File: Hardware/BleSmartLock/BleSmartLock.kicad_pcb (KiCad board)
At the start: 2 copper layers, 119 parts, among them J1 Conn_01x02, J10 Conn_01x04, J11 Conn_01x04, J12 Conn_01x02, J2 Conn_01x01, J3 Conn_01x01, J4 Conn_01x01, J5 Conn_01x01, J6 Conn_ST_STDC14, J7 Conn_01x06, J8 Conn_01x03, J9 Conn_01x04, Q1 PMV50UPE, Q10 NX7002AKA, Q11 PMV50UPE, Q12 NX7002AKA, Q13 NX7002AKA, Q14 NX7002AKA, Q2 PMV50UPE, Q3 NX7002AKA, Q4 PMV50UPE, Q5 NX7002AKA, Q6 NX7002AKA, Q7 PMV50UPE, Q8 NX7002AKA, Q9 PMV50UPE, SW1 SW_Push, U1 RT9086, U2 XC9264b755, U3 BLUENRG-M2SA, U4 LMV611

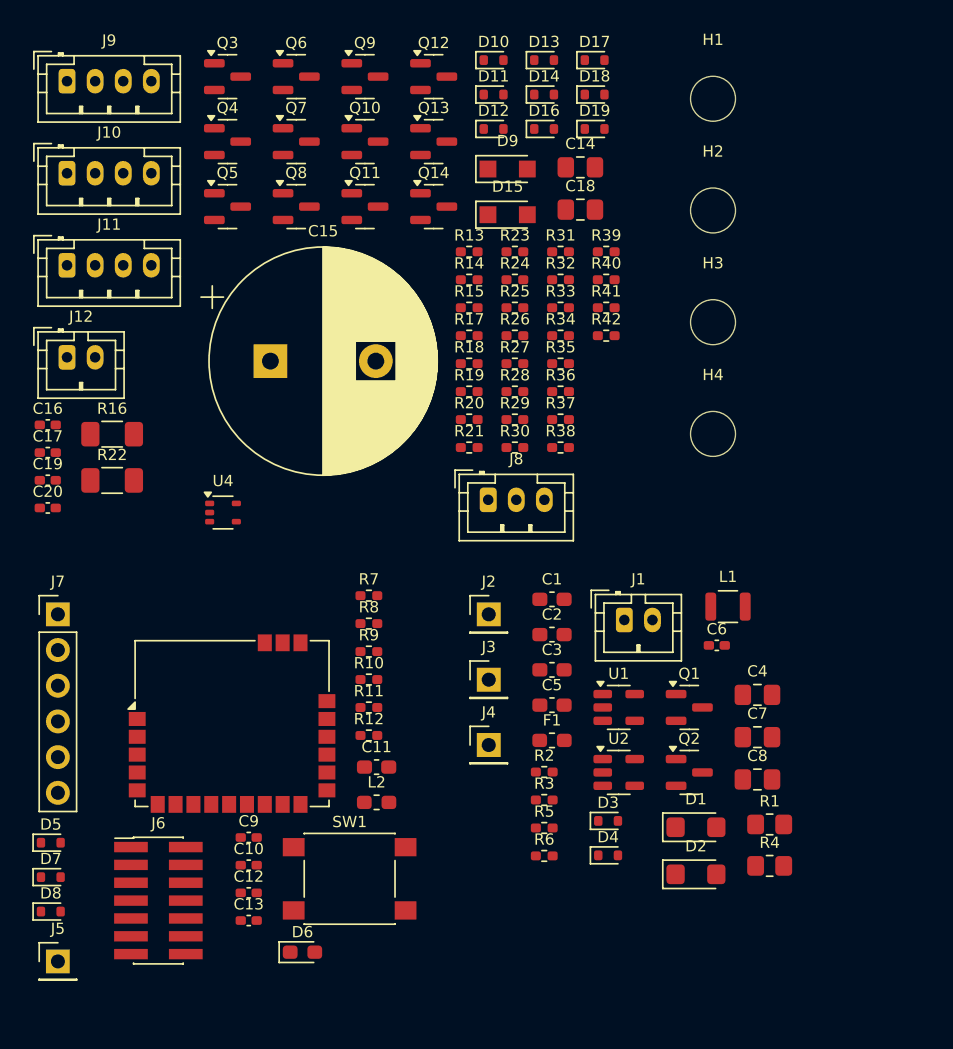
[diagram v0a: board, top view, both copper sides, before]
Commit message: Ajout carte BleSmartLock
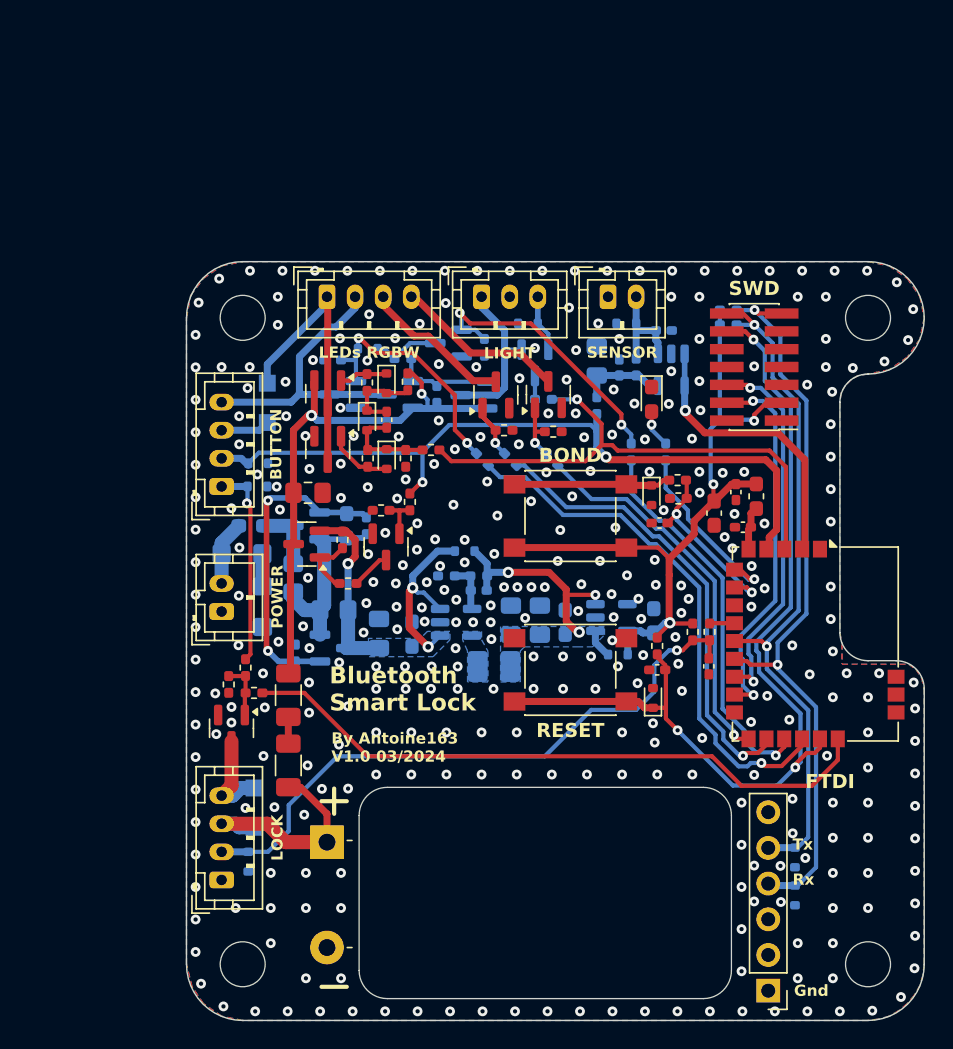
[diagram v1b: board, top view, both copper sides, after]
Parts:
- removed J2, J3, J4, J5: Conn_01x01, Connector_PinHeader_2.54mm:PinHeader_1x01_P2.54mm_Vertical
- removed R42: 160K, Resistor_SMD:R_0402_1005Metric_Pad0.72x0.64mm_HandSolder
- added D20: ESD5Z3.3T1G, Diode_SMD:D_SOD-523, B.Cu at (167.8, 80.9)
- added SW2: SW_Push, Button_Switch_SMD:SW_SPST_PTS645, F.Cu at (163.8, 94.6)
- C1, C18, C19, C2, C20, C3, C4, C5, C6, C7, C8, D1, D2, D3, D4, D8, F1, Q1, Q10, Q11, Q12, Q2, Q5, Q9, R1, R10, R11, R12, R17, R2, R3, R30, R31, R32, R33, R4, R5, R6, U1, U2: moved to B.Cu
- C15: footprint Capacitor_THT:CP_Radial_D16.0mm_P7.50mm -> AM163:CP_Radial_L25.0mm_D16.0mm_P7.50mm_Horizontal_EdgeCuts
- D10, D16: value ESD5Z3.3T1G -> PMEG40T10ER; footprint Diode_SMD:D_SOD-523 -> Diode_SMD:Nexperia_CFP3_SOD-123W; moved to B.Cu
- D11: value EDZVT2R9.1B -> ESD5Z3.3T1G; moved to B.Cu
- D12: value RB501SM-30FH -> EDZVT2R9.1B
- D14: value ESD5Z3.3T1G -> RB501SM-30FH
- D15, D9: value PMEG40T10ER -> ESD5Z3.3T1G; footprint Diode_SMD:Nexperia_CFP3_SOD-123W -> Diode_SMD:D_SOD-523; moved to B.Cu
- D17: value ESD5Z3.3T1G -> ESD5Z3.3T1G; moved to B.Cu
- D18: value RB501SM-30FH -> ESD5Z3.3T1G; moved to B.Cu
- D19: value ESD5Z3.3T1G -> RB501SM-30FH; moved to B.Cu
- D6: value LED -> ESD5Z3.3T1G; footprint LED_SMD:LED_0603_1608Metric_Pad1.05x0.95mm_HandSolder -> Diode_SMD:D_SOD-523
- D7: value ESD5Z3.3T1G -> LED; footprint Diode_SMD:D_SOD-523 -> LED_SMD:LED_0603_1608Metric_Pad1.05x0.95mm_HandSolder
- L1: footprint AM163:L_TDK_VLS252012HBX_Handsoldering -> Inductor_SMD:L_1008_2520Metric_Pad1.43x2.20mm_HandSolder; moved to B.Cu
- Q6: value NX7002AKA -> PMV52ENEA
- R34: value R -> 1K; moved to B.Cu
- R35: value 1K -> 100K; moved to B.Cu
- R36, R38, R40: value 100K -> 1K; moved to B.Cu
- R37, R39: value 1K -> 100K
- R41: value 1K -> 160K; moved to B.Cu
- U4: footprint Package_TO_SOT_SMD:SOT-353_SC-70-5 -> Package_TO_SOT_SMD:SOT-23-5; moved to B.Cu
- moved D17 62.1 mm to (140.9, 119.2), turned to -90 degrees
- moved J7 57.2 mm to (177.9, 128.4), turned to 180 degrees
- moved J6 56.9 mm to (176.9, 84.0), turned to 180 degrees
- moved D10 55.9 mm to (141.3, 115.4), turned to 90 degrees
- moved D9 55.6 mm to (179.8, 121.6), turned to -90 degrees
- moved D7 54.6 mm to (169.6, 86.3), turned to -90 degrees
- moved D8 53.1 mm to (179.8, 118.9), turned to -90 degrees
- moved J10 51.5 mm to (139.0, 120.5), turned to 90 degrees
- moved H4 50.4 mm to (140.5, 126.5)
- moved C17 49.4 mm to (173.7, 105.3), turned to -90 degrees
- moved H3 47.0 mm to (185.0, 126.5)
- moved Q6 46.6 mm to (139.7, 109.7), turned to -90 degrees
- moved C20 45.6 mm to (170.5, 81.4)
- moved C13 44.9 mm to (176.1, 95.4), turned to 180 degrees
- moved C12 44.9 mm to (175.6, 92.9), turned to -90 degrees
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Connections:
- C16 pad 1: Net-(D11-K) -> Net-(D12-K)
- C16 pad 2: Net-(D11-A) -> Net-(D12-A)
- C17 pad 1: Net-(D16-K) -> Net-(D17-K)
- C20 pad 1: Net-(D19-K) -> Net-(D20-K)
- D10 pad 1: /InOut/EX_LIGHT_CMD -> /InOut/COIL_P
- D10 pad 2: GND -> /InOut/COIL_N
- D11 pad 1: Net-(D11-K) -> /InOut/EX_LIGHT_CMD
- D11 pad 2: Net-(D11-A) -> GND
- D12 pad 2: Net-(D11-K) -> Net-(D12-A)
- D13 pad 1: Net-(D11-A) -> Net-(D13-K)
- D13 pad 2: Net-(D13-A) -> Net-(D12-K)
- D14 pad 1: /Bluenrg/EN_IO -> Net-(D12-A)
- D14 pad 2: GND -> Net-(D14-A)
- D15 pad 1: /InOut/BP_LED_P -> /Bluenrg/EN_IO
- D15 pad 2: /InOut/AM_LIGHT_12V_W- -> GND
- D16 pad 1: Net-(D16-K) -> /InOut/BP_LED_P
- D16 pad 2: GND -> /InOut/AM_LIGHT_12V_W-
- D17 pad 1: /InOut/BP_NO -> Net-(D17-K)
- D18 pad 1: Net-(D18-K) -> /InOut/BP_NO
- D18 pad 2: Net-(D18-A) -> GND
- D19 pad 2: GND -> Net-(D19-A)
- D5 pad 1: Net-(D5-K) -> /Bluenrg/M2_~{RESET}
- D6 pad 1: GND -> Net-(D6-K)
- D6 pad 2: Net-(D6-A) -> GND
- D7 pad 1: /Bluenrg/UART_TX -> GND
- D7 pad 2: GND -> Net-(D7-A)
- D8 pad 1: /Bluenrg/UART_RX -> /Bluenrg/UART_TX
- D9 pad 1: /InOut/COIL_P -> /Bluenrg/UART_RX
- D9 pad 2: /InOut/COIL_N -> GND
- J1 pad 1: Net-(D1-A2) -> GND
- J1 pad 2: GND -> Net-(D1-A2)
- J10 pad 2: Net-(D16-K) -> Net-(D17-K)
- J10 pad 3: /InOut/COIL_N -> /InOut/COIL_P
- J10 pad 4: /InOut/COIL_P -> /InOut/COIL_N
- J11 pad 1: /InOut/AM_LIGHT_G -> /InOut/AM_LIGHT_12V_W-
- J11 pad 2: /InOut/AM_LIGHT_R -> /InOut/AM_LIGHT_B_W+
- J11 pad 3: /InOut/AM_LIGHT_B_W+ -> /InOut/AM_LIGHT_G
- J11 pad 4: /InOut/AM_LIGHT_12V_W- -> /InOut/AM_LIGHT_R
- J12 pad 2: Net-(D19-K) -> Net-(D20-K)
- J9 pad 3: /InOut/AM_LIGHT_B_W+ -> /InOut/BP_LED_P
- J9 pad 4: /InOut/BP_LED_P -> /InOut/AM_LIGHT_B_W+
- Q10 pad 1: Net-(D18-A) -> Net-(D19-A)
- Q12 pad 3: Net-(D18-K) -> Net-(D19-K)
- Q7 pad 1: Net-(D12-K) -> Net-(D13-K)
- Q8 pad 1: Net-(D13-A) -> Net-(D14-A)
- R10 pad 2: Net-(D6-A) -> Net-(D7-A)
- R23 pad 2: Net-(D11-A) -> Net-(D12-A)
- R24 pad 2: Net-(D11-K) -> Net-(D12-K)
- R25 pad 1: Net-(D11-A) -> Net-(D12-A)
- R26 pad 1: Net-(D11-K) -> Net-(D12-K)
- R26 pad 2: Net-(D12-K) -> Net-(D13-K)
- R27 pad 1: Net-(D11-A) -> Net-(D12-A)
- R27 pad 2: Net-(D13-A) -> Net-(D14-A)
- R28 pad 2: Net-(D16-K) -> Net-(D17-K)
- R29 pad 1: Net-(D16-K) -> Net-(D17-K)
- R31 pad 2: Net-(D18-K) -> Net-(D19-K)
- R32 pad 1: Net-(D18-A) -> Net-(D19-A)
- R33 pad 2: Net-(D18-A) -> Net-(D19-A)
- R34 pad 1: +3V3 -> /Bluenrg/EN_IO
- R35 pad 1: /Bluenrg/EN_IO -> Net-(Q12-G)
- R35 pad 2: Net-(U4-V+) -> GND
- R36 pad 1: Net-(Q12-G) -> /Bluenrg/LIGHT_WHITE
- R36 pad 2: GND -> Net-(Q12-G)
- R37 pad 1: /Bluenrg/LIGHT_WHITE -> Net-(Q13-G)
- R37 pad 2: Net-(Q12-G) -> GND
- R38 pad 1: Net-(Q13-G) -> /Bluenrg/LIGHT_RED
- R38 pad 2: GND -> Net-(Q13-G)
- R39 pad 1: /Bluenrg/LIGHT_RED -> Net-(Q14-G)
- R39 pad 2: Net-(Q13-G) -> GND
- R40 pad 2: GND -> /Bluenrg/LIGHT_GREEN
- R41 pad 1: Net-(Q14-G) -> Net-(U4-V+)
- R41 pad 2: /Bluenrg/LIGHT_GREEN -> Net-(D20-K)
- R8 pad 1: Net-(D5-K) -> Net-(D6-K)
- SW1 pad 1: +3V3 -> /Bluenrg/M2_~{RESET}
- SW1 pad 2: Net-(D5-K) -> GND
- U3 pad 1: /Bluenrg/ADC2 -> unconnected-(U3-ADC2-Pad1)
- U3 pad 16: /Bluenrg/LIGHT_BLUE -> /Bluenrg/LIGHT_GREEN
- U3 pad 17: /Bluenrg/LIGHT_PWM -> /Bluenrg/LIGHT_WHITE
- U3 pad 18: /Bluenrg/LIGHT_GREEN -> /Bluenrg/LIGHT_BLUE
- U3 pad 20: /Bluenrg/OPENED -> /Bluenrg/~{LOCK}
- U3 pad 3: /Bluenrg/LIGHT_WHITE -> /Bluenrg/LIGHT_PWM
- U3 pad 9: /Bluenrg/~{LOCK} -> /Bluenrg/OPENED
- U4 pad 1: Net-(D19-K) -> Net-(D20-K)
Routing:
- net /Bluenrg/M2_~{RESET}: track 0.00 -> 66.8 mm, vias 0 -> 3
- net /Bluenrg/EN_IO: track 0.00 -> 53.6 mm, vias 0 -> 2
- net /Bluenrg/UART_RX: track 0.00 -> 53.1 mm, vias 0 -> 2
- net +3V3: track 0.00 -> 52.3 mm, vias 0 -> 3
- net /Bluenrg/UART_TX: track 0.00 -> 48.9 mm, vias 0 -> 2
- net /Bluenrg/~{LOCK}: track 0.00 -> 46.0 mm
- net Net-(D17-K): track 0.00 -> 44.4 mm, vias 0 -> 1
- net /InOut/POWER_IO_12V: track 0.00 -> 38.3 mm, vias 0 -> 2
- net /Bluenrg/LIGHT_BLUE: track 0.00 -> 38.3 mm, vias 0 -> 1
- net /Bluenrg/LIGHT_PWM: track 0.00 -> 37.4 mm, vias 0 -> 1
- net /Bluenrg/LIGHT_GREEN: track 0.00 -> 32.5 mm, vias 0 -> 1
- net /Bluenrg/LIGHT_WHITE: track 0.00 -> 27.6 mm, vias 0 -> 1
- net /Bluenrg/LIGHT_RED: track 0.00 -> 27.3 mm, vias 0 -> 1
- net /Bluenrg/M2_SWDIO: track 0.00 -> 26.7 mm, vias 0 -> 2
- net /Bluenrg/M2_SWDCLK: track 0.00 -> 26.7 mm, vias 0 -> 2
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- added copper zone on B.Cu, net +12V
- added copper zone on B.Cu, net /Power/3V6
- added copper zone on B.Cu, net GND
- added copper zone on F.Cu, net GND
- added copper zone on B.Cu, net Net-(U2-Lx)
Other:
- board outline added: 52.5 x 54 mm
- board text added: "BOND"
- board text added: "BUTTON"
- board text added: "Bluetooth Smart Lock"
- board text added: "By Antoine163 V1.0 03/2024"
- board text added: "FTDI"
- board text added: "Gnd"
- board text added: "LEDs RGBW"
- board text added: "LIGHT"
- board text added: "LOCK"
- board text added: "POWER"
- board text added: "RESET"
- board text added: "Rx"
- board text added: "SENSOR"
- board text added: "SWD"
- board text added: "Tx"

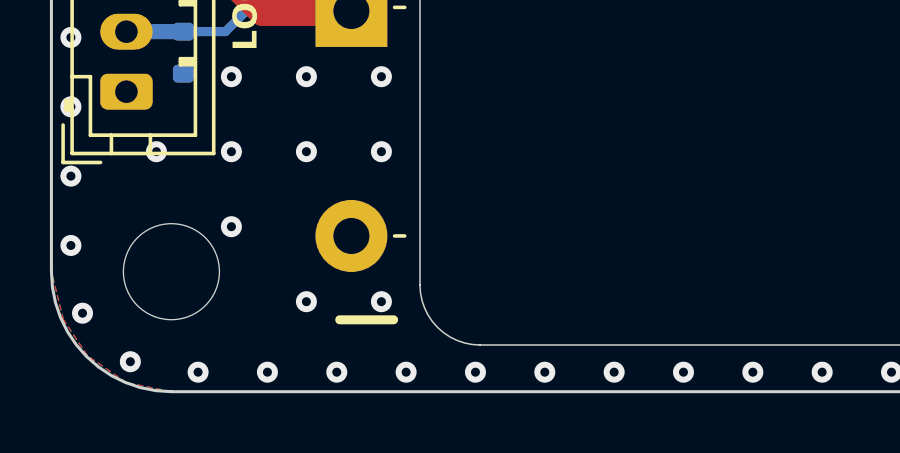
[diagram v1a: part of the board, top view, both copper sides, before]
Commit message: Ajout fichier de production et bom interactive
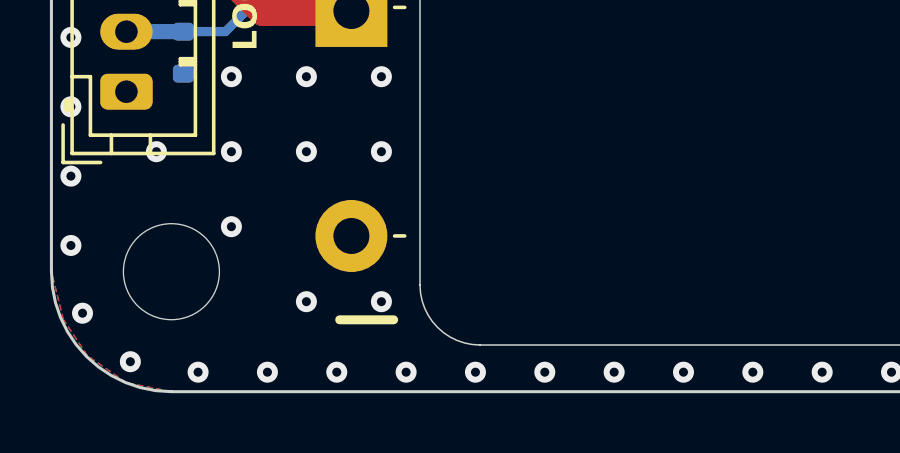
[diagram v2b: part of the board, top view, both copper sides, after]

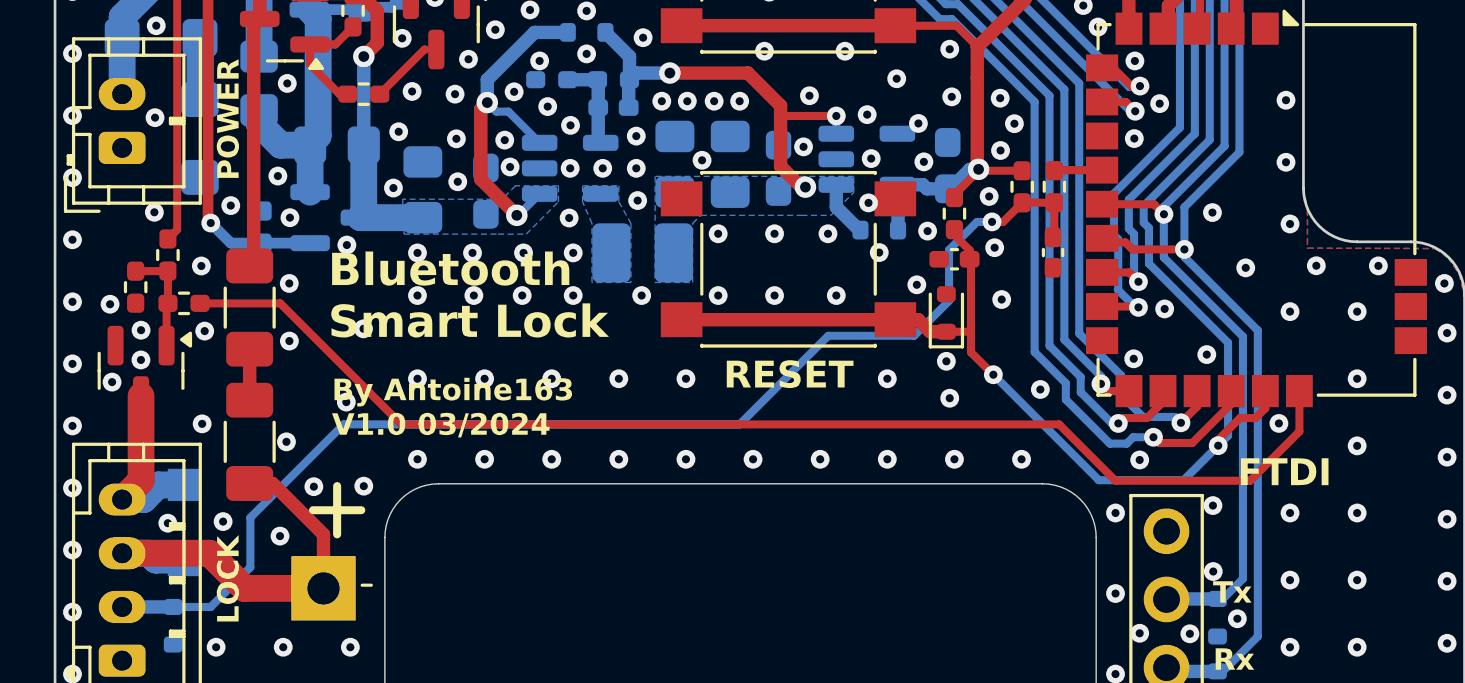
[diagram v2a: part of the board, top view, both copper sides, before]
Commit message: Mise a jour pcb en v1.1 et readme
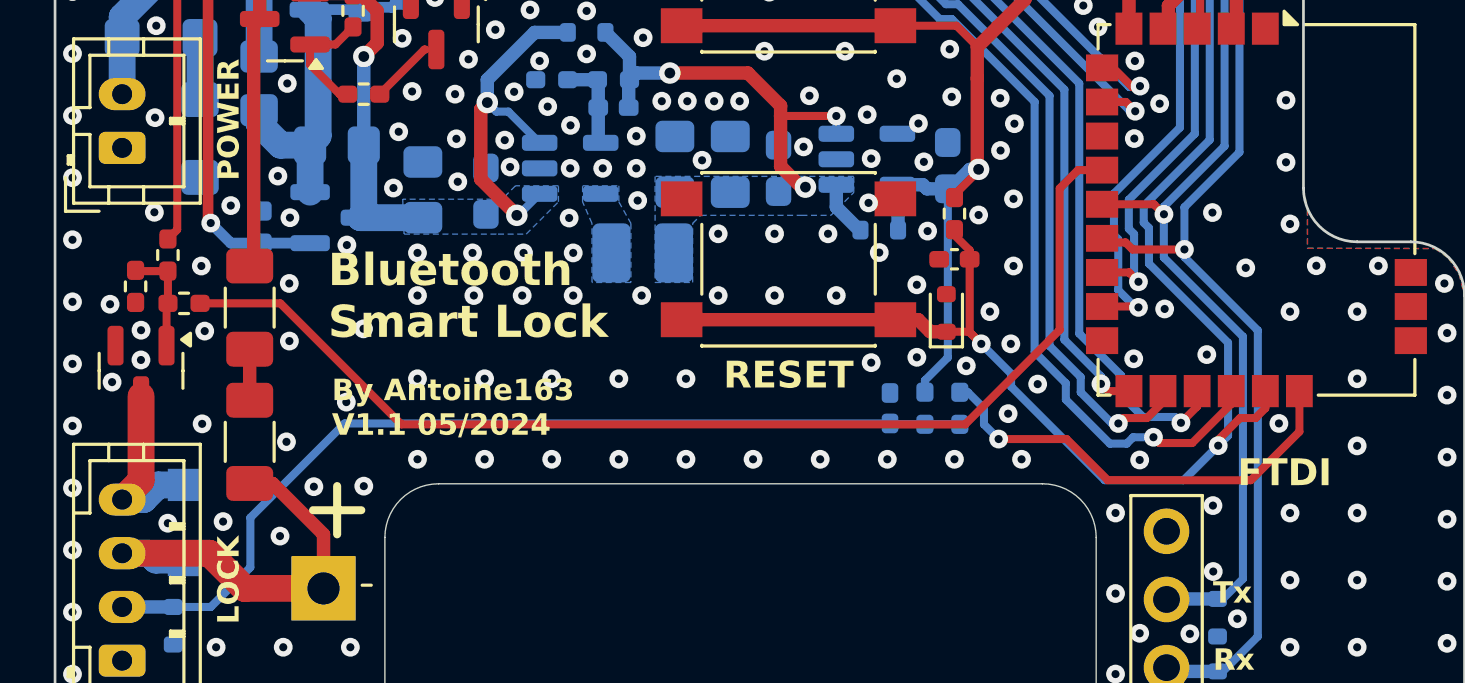
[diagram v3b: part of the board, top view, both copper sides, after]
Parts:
- C17, R28, R29: moved to B.Cu
- moved R29 9.01 mm to (168.9, 111.1)
- moved R28 8.97 mm to (170.2, 111.1)
- moved C17 8.40 mm to (167.6, 111.1), turned to 90 degrees
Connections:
- U3 pad 20: /Bluenrg/~{LOCK} -> /Bluenrg/OPENED
- U3 pad 9: /Bluenrg/OPENED -> /Bluenrg/~{LOCK}
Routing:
- net /Bluenrg/OPENED: track 1.48 -> 16.6 mm, vias 0 -> 1
- net Net-(D17-K): track 44.4 -> 35.1 mm, vias 1 -> 0
- net +3V3: track 52.3 -> 58.7 mm
- net /Bluenrg/~{LOCK}: track 46.0 -> 42.5 mm
- net GND: vias 334 -> 337
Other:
- board text added: "By Antoine163 V1.1 05/2024"
- board text removed: "By Antoine163 V1.0 03/2024"
